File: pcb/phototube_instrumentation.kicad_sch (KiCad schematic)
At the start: 35 parts, among them K1 DIPxx-1Axx-11x, K4 DIPxx-1Axx-11x, K5 DIPxx-1Axx-11x, K7 DIPxx-1Axx-11x, U11 OPA1612AxD, U12 OPA140, U6 OPA140, U6 OPA1612AxD, U9 OPA1612AxD

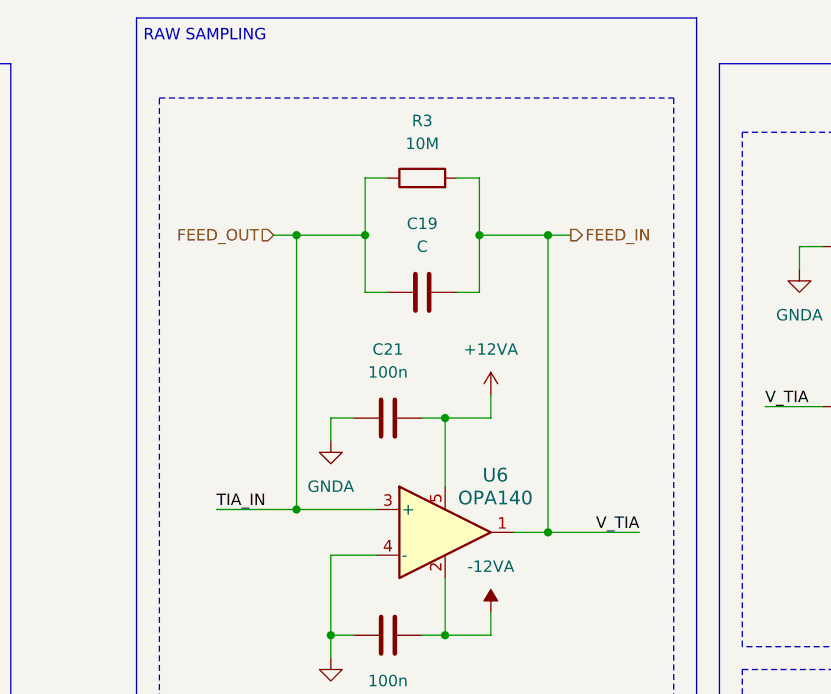
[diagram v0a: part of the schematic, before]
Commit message: reworked the digital isolation block
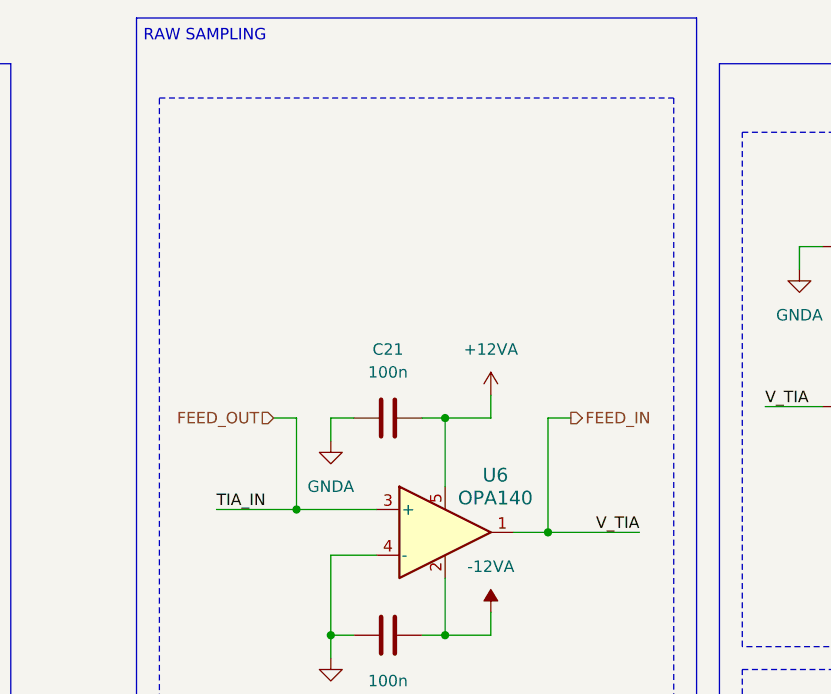
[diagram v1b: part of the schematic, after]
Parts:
- removed C19: C, symbol Device:C
- removed R3: 10M, symbol Device:R

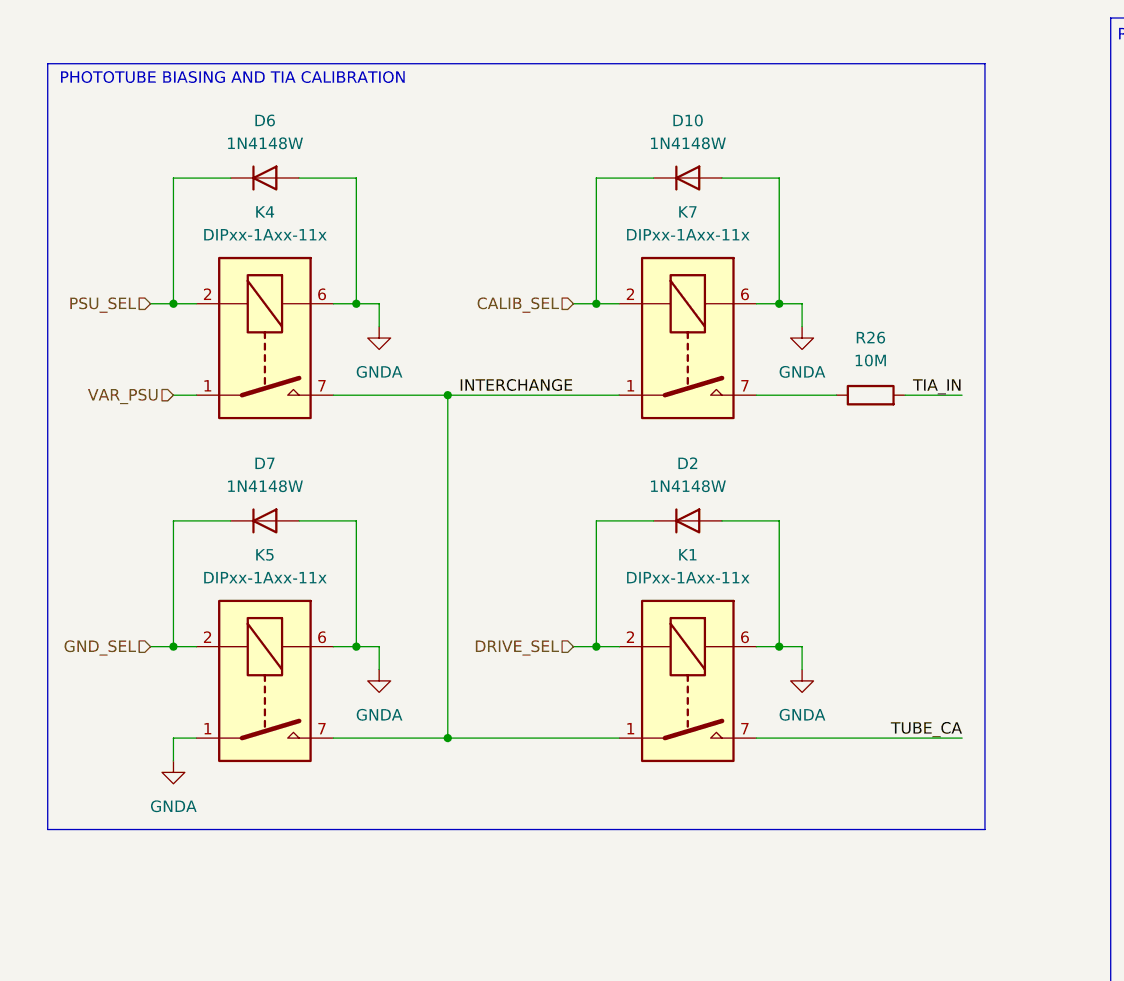
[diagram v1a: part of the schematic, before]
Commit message: rework to tia feedback selection, board power, and ui
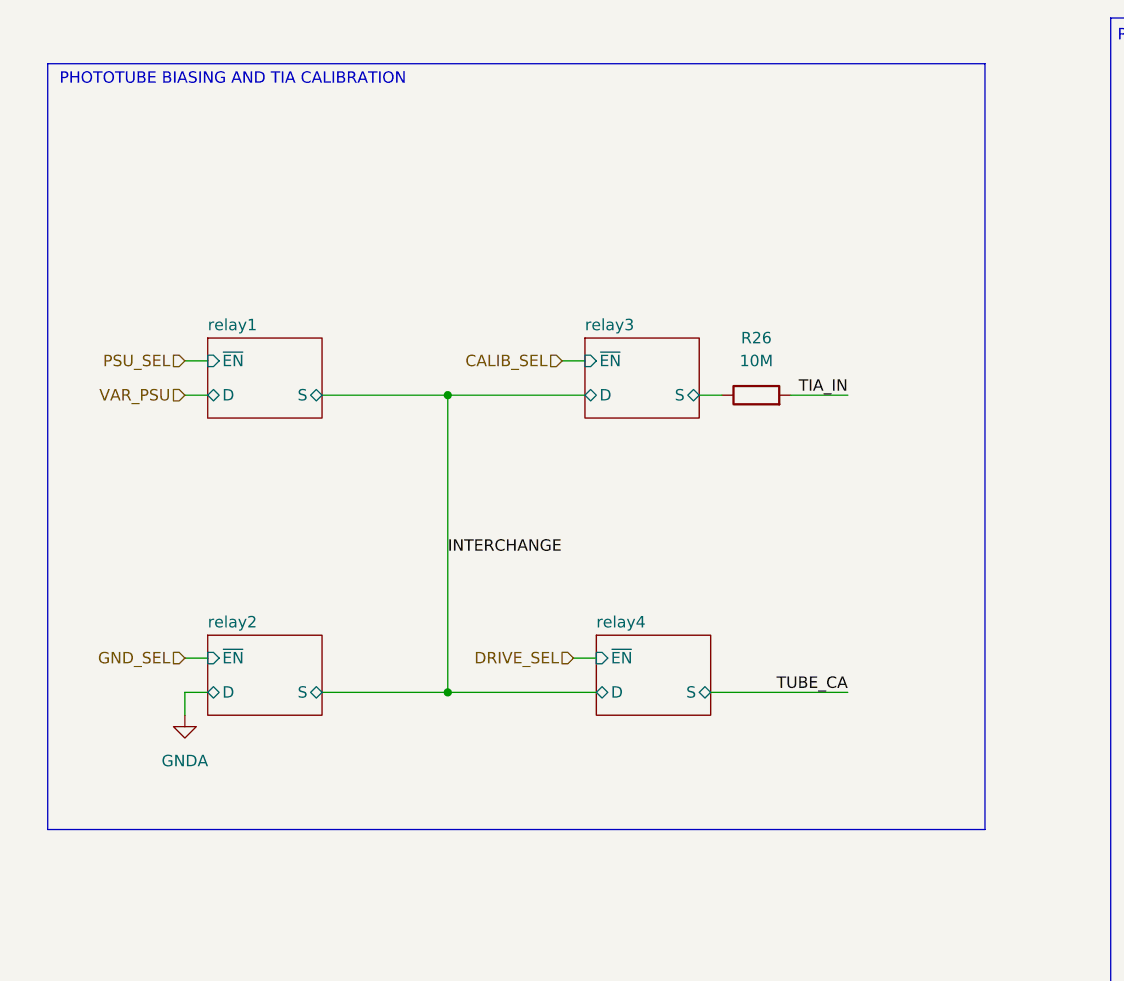
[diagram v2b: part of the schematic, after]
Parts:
- removed D10, D2, D6, D7: 1N4148W, Diode_SMD:D_SOD-123, symbol Diode:1N4148W
- removed K1, K4, K5, K7: DIPxx-1Axx-11x, Relay_THT:Relay_StandexMeder_DIP_LowProfile, symbol Relay:DIPxx-1Axx-11x
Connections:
- net relay3/S: now reaches R26.1
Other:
- added sheet relay1 (relay.kicad_sch)
- added sheet relay2 (relay.kicad_sch)
- added sheet relay3 (relay.kicad_sch)
- added sheet relay4 (relay.kicad_sch)
- moved on the sheet: R26
